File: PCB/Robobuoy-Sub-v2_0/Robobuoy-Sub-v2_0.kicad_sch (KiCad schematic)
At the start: 6 parts

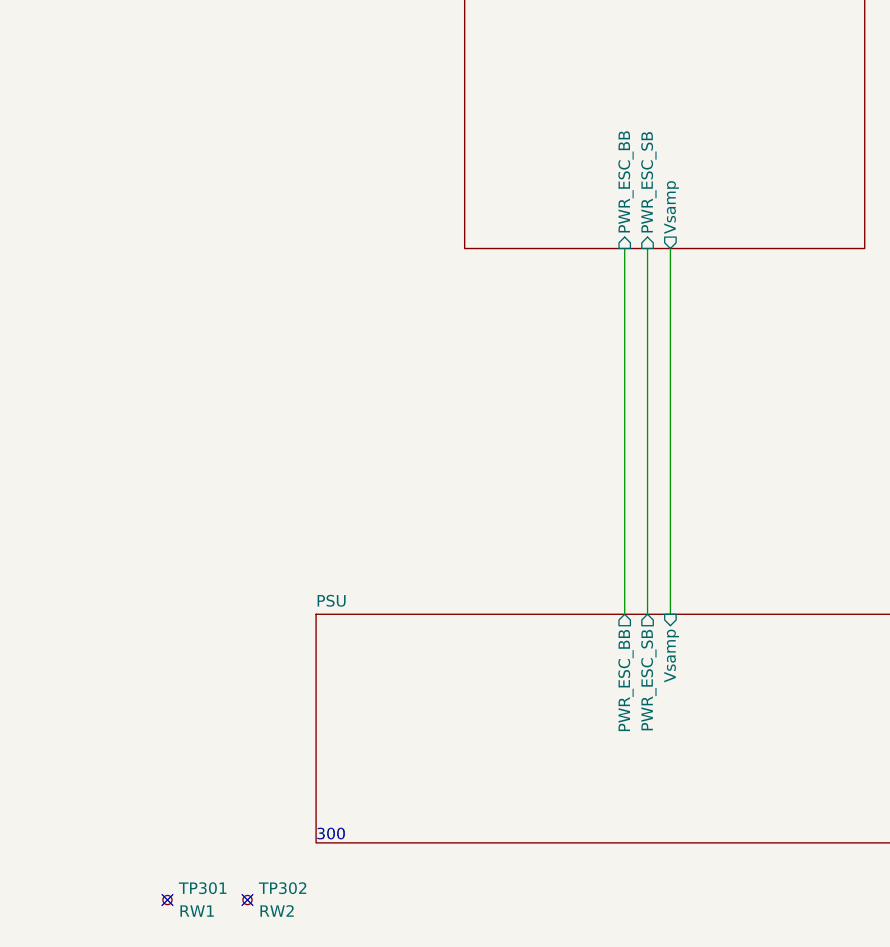
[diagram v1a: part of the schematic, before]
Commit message: Struct re defined. not finished yet
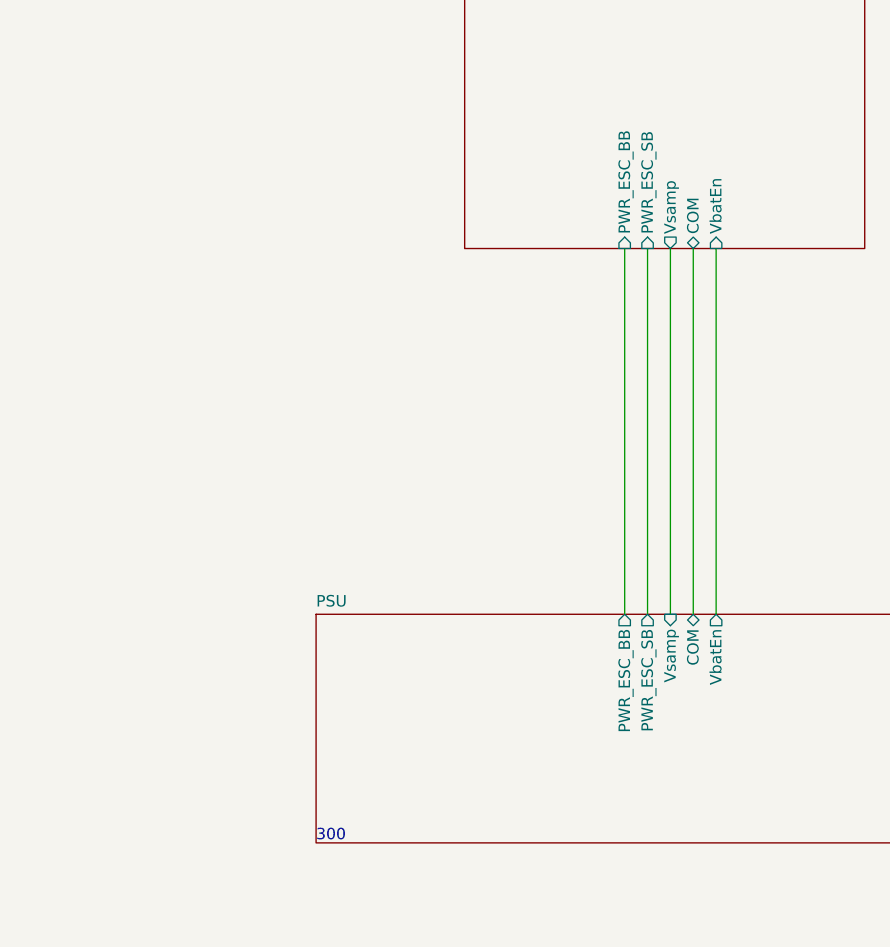
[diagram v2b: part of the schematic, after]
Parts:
- removed TP301: RW1, A_Misc:ReworkPins, symbol Connector:TestPoint_Small
- removed TP302: RW2, A_Misc:ReworkPins, symbol Connector:TestPoint_Small
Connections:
- no-connect marks 2 -> 0
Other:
- sheet CPU ports: added COM, VbatEn; removed none
- sheet PSU ports: added COM, VbatEn; removed none
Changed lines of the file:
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@@
 		(company "NicE Engineering")
 	)
-	(no_connect
-		(at 62.23 193.04)
-	)
-	(no_connect
-		(at 71.12 193.04)
+	(wire
+		(pts
+			(xy 120.65 120.65) (xy 120.65 161.29)
+		)
+		(stroke
+			(width 0)
+			(type default)
+		)
+	)
+	(wire
+		(pts
+			(xy 123.19 120.65) (xy 123.19 161.29)
+		)
+		(stroke
+			(width 0)
+			(type default)
+		)
 	)
 	(wire
@@
 			)
 			(justify left bottom)
-		)
-	)
-	(symbol
-		(lib_id "Connector:TestPoint_Small")
-		(at 71.12 193.04 0)
-		(unit 1)
-		(exclude_from_sim no)
-		(in_bom no)
-		(on_board yes)
-		(dnp no)
-		(fields_autoplaced yes)
-		(property "Reference" "TP302"
-			(at 72.39 191.77 0)
-			(effects
-				(font
-					(size 1.27 1.27)
-				)
-				(justify left)
-			)
-		)
-		(property "Value" "RW2"
-			(at 72.39 194.31 0)
-			(effects
-				(font
-					(size 1.27 1.27)
-				)
-				(justify left)
-			)
-		)
-		(property "Footprint" "A_Misc:ReworkPins"
-			(at 76.2 193.04 0)
-			(effects
-				(font
-					(size 1.27 1.27)
-				)
-				(hide yes)
-			)
-		)
-		(property "Datasheet" "~"
-			(at 76.2 193.04 0)
-			(effects
-				(font
-					(size 1.27 1.27)
-				)
-				(hide yes)
-			)
-		)
-		(property "Description" ""
-			(at 71.12 193.04 0)
-			(effects
-				(font
-					(size 1.27 1.27)
-				)
-				(hide yes)
-			)
-		)
-		(pin "1"
-		)
-		(instances
-			(project "Robuoy-Sub"
-				(path "/77bea089-a6ae-4a6f-b95b-7a9010ad7c5d"
-					(reference "TP302")
-					(unit 1)
-				)
-			)
 		)
 	)
@@
 	)
 	(symbol
-		(lib_id "Connector:TestPoint_Small")
-		(at 62.23 193.04 0)
-		(unit 1)
-		(exclude_from_sim no)
-		(in_bom no)
-		(on_board yes)
-		(dnp no)
-		(fields_autoplaced yes)
-		(property "Reference" "TP301"
-			(at 63.5 191.77 0)
-			(effects
-				(font
-					(size 1.27 1.27)
-				)
-				(justify left)
-			)
-		)
-		(property "Value" "RW1"
-			(at 63.5 194.31 0)
-			(effects
-				(font
-					(size 1.27 1.27)
-				)
-				(justify left)
-			)
-		)
-		(property "Footprint" "A_Misc:ReworkPins"
-			(at 67.31 193.04 0)
-			(effects
-				(font
-					(size 1.27 1.27)
-				)
-				(hide yes)
-			)
-		)
-		(property "Datasheet" "~"
-			(at 67.31 193.04 0)
-			(effects
-				(font
-					(size 1.27 1.27)
-				)
-				(hide yes)
-			)
-		)
-		(property "Description" ""
-			(at 62.23 193.04 0)
-			(effects
-				(font
-					(size 1.27 1.27)
-				)
-				(hide yes)
-			)
-		)
-		(pin "1"
-		)
-		(instances
-			(project "Robuoy-Sub"
-				(path "/77bea089-a6ae-4a6f-b95b-7a9010ad7c5d"
-					(reference "TP301")
-					(unit 1)
-				)
-			)
-		)
-	)
-	(symbol
 		(lib_id "Mechanical:MountingHole")
 		(at 21.59 190.5 0)
@@
 			)
 		)
+		(pin "COM" bidirectional
+			(at 120.65 120.65 270)
+			(effects
+				(font
+					(size 1.27 1.27)
+				)
+				(justify left)
+			)
+		)
+		(pin "VbatEn" input
+			(at 123.19 120.65 270)
+			(effects
+				(font
+					(size 1.27 1.27)
+				)
+				(justify left)
+			)
+		)
 		(instances
 			(project "Robobuoy-Sub-v2_0"
@@
 			(effects
 				(font
+					(size 1.27 1.27)
+				)
+				(justify right)
+			)
+		)
+		(pin "COM" bidirectional
+			(at 120.65 161.29 90)
+			(effects
+				(font
+					(size 1.27 1.27)
+				)
+				(justify right)
+			)
+		)
+		(pin "VbatEn" output
+			(at 123.19 161.29 90)
+			(effects
+				(font

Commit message: Many changes
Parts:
- renumbered H301 to H501, H302 to H502, H303 to H503, H304 to H504
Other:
- added sheet ESC_BB (esc_bb.kicad_sch)
- added sheet ESC_SB (esc.kicad_sch)
- sheet CPU ports: added PwrEn; removed none
- sheet PSU ports: added PwrEn; removed none
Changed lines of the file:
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@@
+	(wire
+		(pts
+			(xy 125.73 120.65) (xy 125.73 161.29)
+		)
+		(stroke
+			(width 0)
+			(type default)
+		)
+	)
 	(wire
 		(pts
@@
 		(on_board yes)
 		(dnp no)
-		(property "Reference" "H304"
+		(property "Reference" "H504"
 			(at 28.575 187.325 0)
 			(effects
@@
 		)
 		(property "JLCS" ""
+			(at 31.75 190.5 0)
+			(effects
+				(font
+					(size 1.27 1.27)
+				)
+				(hide yes)
+			)
+		)
+		(property "Field5" ""
+			(at 31.75 190.5 0)
+			(effects
+				(font
+					(size 1.27 1.27)
+				)
+				(hide yes)
+			)
+		)
+		(property "Type" ""
 			(at 31.75 190.5 0)
 			(effects
@@
 			(project "Robuoy-Sub"
 				(path "/77bea089-a6ae-4a6f-b95b-7a9010ad7c5d"
-					(reference "H304")
+					(reference "H504")
 					(unit 1)
 				)
@@
 		(on_board yes)
 		(dnp no)
-		(property "Reference" "H303"
+		(property "Reference" "H503"
 			(at 24.13 184.785 0)
 			(effects
@@
 		)
 		(property "JLCS" ""
+			(at 26.67 190.5 0)
+			(effects
+				(font
+					(size 1.27 1.27)
+				)
+				(hide yes)
+			)
+		)
+		(property "Field5" ""
+			(at 26.67 190.5 0)
+			(effects
+				(font
+					(size 1.27 1.27)
+				)
+				(hide yes)
+			)
+		)
+		(property "Type" ""
 			(at 26.67 190.5 0)
 			(effects
@@
 			(project "Robuoy-Sub"
 				(path "/77bea089-a6ae-4a6f-b95b-7a9010ad7c5d"
-					(reference "H303")
+					(reference "H503")
 					(unit 1)
 				)
@@
 		(on_board yes)
 		(dnp no)
-		(property "Reference" "H302"
+		(property "Reference" "H502"
 			(at 18.415 187.325 0)
 			(effects
@@
 		)
 		(property "JLCS" ""
+			(at 21.59 190.5 0)
+			(effects
+				(font
+					(size 1.27 1.27)
+				)
+				(hide yes)
+			)
+		)
+		(property "Field5" ""
+			(at 21.59 190.5 0)
+			(effects
+				(font
+					(size 1.27 1.27)
+				)
+				(hide yes)
+			)
+		)
+		(property "Type" ""
 			(at 21.59 190.5 0)
 			(effects
@@
 			(project "Robuoy-Sub"
 				(path "/77bea089-a6ae-4a6f-b95b-7a9010ad7c5d"
-					(reference "H302")
+					(reference "H502")
 					(unit 1)
 				)
@@
 		(on_board yes)
 		(dnp no)
-		(property "Reference" "H301"
+		(property "Reference" "H501"
 			(at 12.7 184.785 0)
 			(effects
@@
 		)
 		(property "JLCS" ""
+			(at 16.51 190.5 0)
+			(effects
+				(font
+					(size 1.27 1.27)
+				)
+				(hide yes)
+			)
+		)
+		(property "Field5" ""
+			(at 16.51 190.5 0)
+			(effects
+				(font
+					(size 1.27 1.27)
+				)
+				(hide yes)
+			)
+		)
+		(property "Type" ""
 			(at 16.51 190.5 0)
 			(effects
@@
 			(project "Robuoy-Sub"
 				(path "/77bea089-a6ae-4a6f-b95b-7a9010ad7c5d"
-					(reference "H301")
+					(reference "H501")
 					(unit 1)
 				)
@@
 			)
 		)
+		(pin "PwrEn" input
+			(at 125.73 120.65 270)
+			(effects
+				(font
+					(size 1.27 1.27)
+				)
+				(justify left)
+			)
+		)
 		(instances
 			(project "Robobuoy-Sub-v2_0"
@@
 	)
 	(sheet
+		(at 182.88 85.09)
+		(size 34.925 12.065)
+		(fields_autoplaced yes)
+		(stroke
+			(width 0.1524)
+			(type solid)
+		)
+		(fill
+			(color 0 0 0 0.0000)
+		)
+		(property "Sheetname" "ESC_BB"
+			(at 182.88 84.3784 0)
+			(effects
+				(font
+					(size 1.27 1.27)
+				)
+				(justify left bottom)
+			)
+		)
+		(property "Sheetfile" "esc_bb.kicad_sch"
+			(at 182.88 97.7396 0)
+			(effects
+				(font
+					(size 1.27 1.27)
+				)
+				(justify left top)
+				(hide yes)
+			)
+		)
+		(instances
+			(project "Robobuoy-Sub-v2_0"
+				(path "/77bea089-a6ae-4a6f-b95b-7a9010ad7c5d"
+					(page "5")
+				)
+			)
+		)
+	)
+	(sheet
+		(at 182.88 65.405)
+		(size 34.925 11.43)
+		(fields_autoplaced yes)
+		(stroke
+			(width 0.1524)
+			(type solid)
+		)
+		(fill
+			(color 0 0 0 0.0000)
+		)
+		(property "Sheetname" "ESC_SB"
+			(at 182.88 64.6934 0)
+			(effects
+				(font
+					(size 1.27 1.27)
+				)
+				(justify left bottom)
+			)
+		)
+		(property "Sheetfile" "esc.kicad_sch"
+			(at 182.88 77.4196 0)
+			(effects
+				(font
+					(size 1.27 1.27)
+				)
+				(justify left top)
+				(hide yes)
+			)
+		)
+		(instances
+			(project "Robobuoy-Sub-v2_0"
+				(path "/77bea089-a6ae-4a6f-b95b-7a9010ad7c5d"
+					(page "4")
+				)
+			)
+		)
+	)
+	(sheet
 		(at 78.74 161.29)
 		(size 69.85 25.4)
@@
 			(effects
 				(font
+					(size 1.27 1.27)
+				)
+				(justify right)
+			)
+		)
+		(pin "PwrEn" output
+			(at 125.73 161.29 90)
+			(effects
+				(font

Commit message: Pcb changes
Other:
- sheet CPU ports: added ESC_BB, ESC_PWR_BB, ESC_PWR_SB, ESC_SB; removed none
- sheet ESC_BB: file esc_bb.kicad_sch -> esc2.0.kicad_sch
- sheet ESC_BB ports: added ESC_PWR, ESCin; removed none
- sheet ESC_SB: file esc.kicad_sch -> esc2.0.kicad_sch
- sheet ESC_SB ports: added ESC_PWR, ESCin; removed none
- note added: "ESP32 COMPASS BATTERY MONITOR POWERSUPPY 3.3V"
- note removed: "ESP32 COMPASS BATTERY MONITOR POWERSUPPY 12V 5V 3.3V"
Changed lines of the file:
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@@
 (kicad_sch
-	(version 20231120)
+	(version 20241209)
 	(generator "eeschema")
-	(generator_version "8.0")
+	(generator_version "9.0")
 	(paper "A4")
 	(title_block
@@
 		(company "NicE Engineering")
 	)
-	(wire
-		(pts
-			(xy 125.73 120.65) (xy 125.73 161.29)
-		)
-		(stroke
-			(width 0)
-			(type default)
-		)
-	)
-	(wire
-		(pts
-			(xy 120.65 120.65) (xy 120.65 161.29)
-		)
-		(stroke
-			(width 0)
-			(type default)
-		)
-	)
-	(wire
-		(pts
-			(xy 123.19 120.65) (xy 123.19 161.29)
-		)
-		(stroke
-			(width 0)
-			(type default)
-		)
-	)
-	(wire
-		(pts
-			(xy 115.57 120.65) (xy 115.57 161.29)
-		)
-		(stroke
-			(width 0)
-			(type default)
-		)
-	)
-	(wire
-		(pts
-			(xy 113.03 120.65) (xy 113.03 161.29)
-		)
-		(stroke
-			(width 0)
-			(type default)
-		)
-	)
-	(wire
-		(pts
-			(xy 118.11 120.65) (xy 118.11 161.29)
-		)
-		(stroke
-			(width 0)
-			(type default)
-		)
-	)
 	(text "300"
 		(exclude_from_sim no)
@@
 		)
 	)
-	(text "ESP32\nCOMPASS\nBATTERY MONITOR\nPOWERSUPPY 12V 5V 3.3V\n"
+	(text "ESP32\nCOMPASS\nBATTERY MONITOR\nPOWERSUPPY 3.3V\n"
 		(exclude_from_sim no)
 		(at 13.462 22.352 0)
@@
 			)
 			(justify left bottom)
+		)
+	)
+	(wire
+		(pts
+			(xy 139.7 81.28) (xy 179.07 81.28)
+		)
+		(stroke
+			(width 0)
+			(type default)
+		)
+	)
+	(wire
+		(pts
+			(xy 139.7 85.09) (xy 179.07 85.09)
+		)
+		(stroke
+			(width 0)
+			(type default)
+		)
+	)
+	(wire
+		(pts
+			(xy 125.73 120.65) (xy 125.73 161.29)
+		)
+		(stroke
+			(width 0)
+			(type default)
+		)
+	)
+	(wire
+		(pts
+			(xy 120.65 120.65) (xy 120.65 161.29)
+		)
+		(stroke
+			(width 0)
+			(type default)
+		)
+	)
+	(wire
+		(pts
+			(xy 139.7 60.96) (xy 179.07 60.96)
+		)
+		(stroke
+			(width 0)
+			(type default)
+		)
+	)
+	(wire
+		(pts
+			(xy 139.7 64.77) (xy 179.07 64.77)
+		)
+		(stroke
+			(width 0)
+			(type default)
+		)
+	)
+	(wire
+		(pts
+			(xy 123.19 120.65) (xy 123.19 161.29)
+		)
+		(stroke
+			(width 0)
+			(type default)
+		)
+	)
+	(wire
+		(pts
+			(xy 115.57 120.65) (xy 115.57 161.29)
+		)
+		(stroke
+			(width 0)
+			(type default)
+		)
+	)
+	(wire
+		(pts
+			(xy 113.03 120.65) (xy 113.03 161.29)
+		)
+		(stroke
+			(width 0)
+			(type default)
+		)
+	)
+	(wire
+		(pts
+			(xy 118.11 120.65) (xy 118.11 161.29)
+		)
+		(stroke
+			(width 0)
+			(type default)
 		)
 	)
@@
 		(at 95.25 50.8)
 		(size 44.45 69.85)
+		(exclude_from_sim no)
+		(in_bom yes)
+		(on_board yes)
+		(dnp no)
 		(fields_autoplaced yes)
 		(stroke
@@
 				)
 				(justify left)
+			)
+		)
+		(pin "ESC_BB" output
+			(at 139.7 60.96 0)
+			(effects
+				(font
+					(size 1.27 1.27)
+				)
+				(justify right)
+			)
+		)
+		(pin "ESC_SB" output
+			(at 139.7 81.28 0)
+			(effects
+				(font
+					(size 1.27 1.27)
+				)
+				(justify right)
+			)
+		)
+		(pin "ESC_PWR_BB" output
+			(at 139.7 64.77 0)
+			(effects
+				(font
+					(size 1.27 1.27)
+				)
+				(justify right)
+			)
+		)
+		(pin "ESC_PWR_SB" output
+			(at 139.7 85.09 0)
+			(effects
+				(font
+					(size 1.27 1.27)
+				)
+				(justify right)
 			)
 		)
@@
 	)
 	(sheet
-		(at 182.88 85.09)
-		(size 34.925 12.065)
+		(at 179.07 57.15)
+		(size 28.575 12.7)
+		(exclude_from_sim no)
+		(in_bom yes)
+		(on_board yes)
+		(dnp no)
 		(fields_autoplaced yes)
 		(stroke
@@
 		)
 		(property "Sheetname" "ESC_BB"
-			(at 182.88 84.3784 0)
+			(at 179.07 56.4384 0)
 			(effects
 				(font
@@
 			)
 		)
-		(property "Sheetfile" "esc_bb.kicad_sch"
-			(at 182.88 97.7396 0)
+		(property "Sheetfile" "esc2.0.kicad_sch"
+			(at 179.07 70.4346 0)
 			(effects
 				(font
@@
 				)
 				(justify left top)
-				(hide yes)
+			)
+		)
+		(pin "ESCin" output
+			(at 179.07 60.96 180)
+			(effects
+				(font
+					(size 1.27 1.27)
+				)
+				(justify left)
+			)
+		)
+		(pin "ESC_PWR" output
+			(at 179.07 64.77 180)
+			(effects
+				(font
+					(size 1.27 1.27)
+				)
+				(justify left)
 			)
 		)
@@
 			(project "Robobuoy-Sub-v2_0"
 				(path "/77bea089-a6ae-4a6f-b95b-7a9010ad7c5d"
-					(page "5")
-				)
-			)
-		)
-	)
-	(sheet
-		(at 182.88 65.405)
-		(size 34.925 11.43)
-		(fields_autoplaced yes)
-		(stroke
-			(width 0.1524)
-			(type solid)
-		)
-		(fill
-			(color 0 0 0 0.0000)
-		)
-		(property "Sheetname" "ESC_SB"
-			(at 182.88 64.6934 0)
-			(effects
-				(font
-					(size 1.27 1.27)
-				)
-				(justify left bottom)
-			)
-		)
-		(property "Sheetfile" "esc.kicad_sch"
-			(at 182.88 77.4196 0)
-			(effects
-				(font
-					(size 1.27 1.27)
-				)
-				(justify left top)
-				(hide yes)
-			)
-		)
-		(instances
-			(project "Robobuoy-Sub-v2_0"
-				(path "/77bea089-a6ae-4a6f-b95b-7a9010ad7c5d"
-					(page "4")
+					(page "6")
 				)
 			)
@@
 		(at 78.74 161.29)
 		(size 69.85 25.4)
+		(exclude_from_sim no)
+		(in_bom yes)
+		(on_board yes)
+		(dnp no)
 		(fields_autoplaced yes)
 		(stroke
@@
 		)
 	)
+	(sheet
+		(at 179.07 77.47)
+		(size 28.575 12.7)
+		(exclude_from_sim no)
+		(in_bom yes)
+		(on_board yes)
+		(dnp no)
+		(fields_autoplaced yes)
+		(stroke
+			(width 0.1524)
+			(type solid)
+		)
+		(fill
+			(color 0 0 0 0.0000)
+		)
+		(property "Sheetname" "ESC_SB"
+			(at 179.07 76.7584 0)
+			(effects
+				(font
+					(size 1.27 1.27)
+				)
+				(justify left bottom)
+			)
+		)
+		(property "Sheetfile" "esc2.0.kicad_sch"
+			(at 179.07 90.7546 0)
+			(effects
+				(font
+					(size 1.27 1.27)
+				)
+				(justify left top)
+			)
+		)
+		(pin "ESCin" output
+			(at 179.07 81.28 180)
+			(effects
+				(font
+					(size 1.27 1.27)
+				)
+				(justify left)
+			)
+		)
+		(pin "ESC_PWR" output
+			(at 179.07 85.09 180)
+			(effects
+				(font
+					(size 1.27 1.27)
+				)
+				(justify left)
+			)
+		)
+		(instances
+			(project "Robobuoy-Sub-v2_0"
+				(path "/77bea089-a6ae-4a6f-b95b-7a9010ad7c5d"
+					(page "3")
+				)
+			)
+		)
+	)
 	(sheet_instances
 		(path "/"
@@
 		)
 	)
+	(embedded_fonts no)
 )
